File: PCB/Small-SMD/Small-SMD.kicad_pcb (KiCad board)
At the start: 2 copper layers, 65.1 x 96.9 mm, 28 parts, among them J1 Daisy port in, J3 UART, J4 Daisy port out, K1 HYC77-TF09-200, U1 PC817C-S, U2 SE5218, U21 TXB0104QPWRQ1

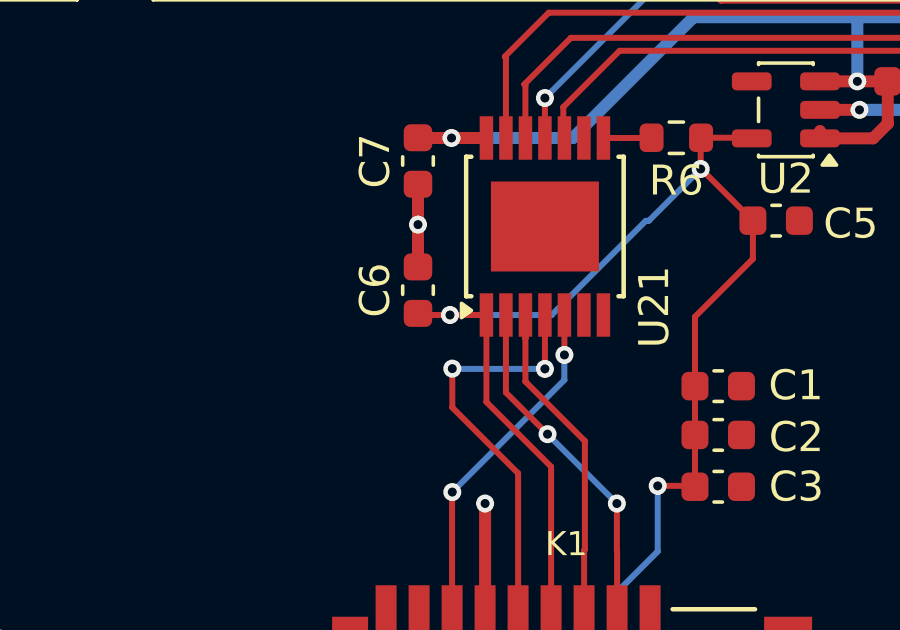
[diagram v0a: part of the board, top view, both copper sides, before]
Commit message: Switch to cheaper IDC box header
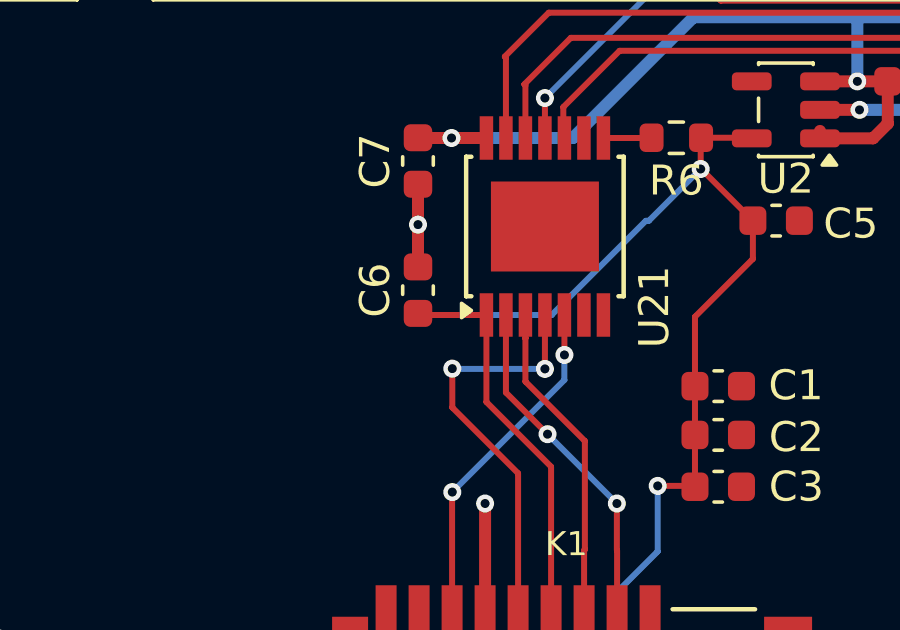
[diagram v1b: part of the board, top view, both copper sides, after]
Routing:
- net 3V3: vias 4 -> 3
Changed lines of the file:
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@@
-	)
-	(via
-		(at 115.5556 116.8078)
-		(size 0.6)
-		(drill 0.3)
-		(layers "F.Cu" "B.Cu")
-		(net 42)
 	)
 	(via

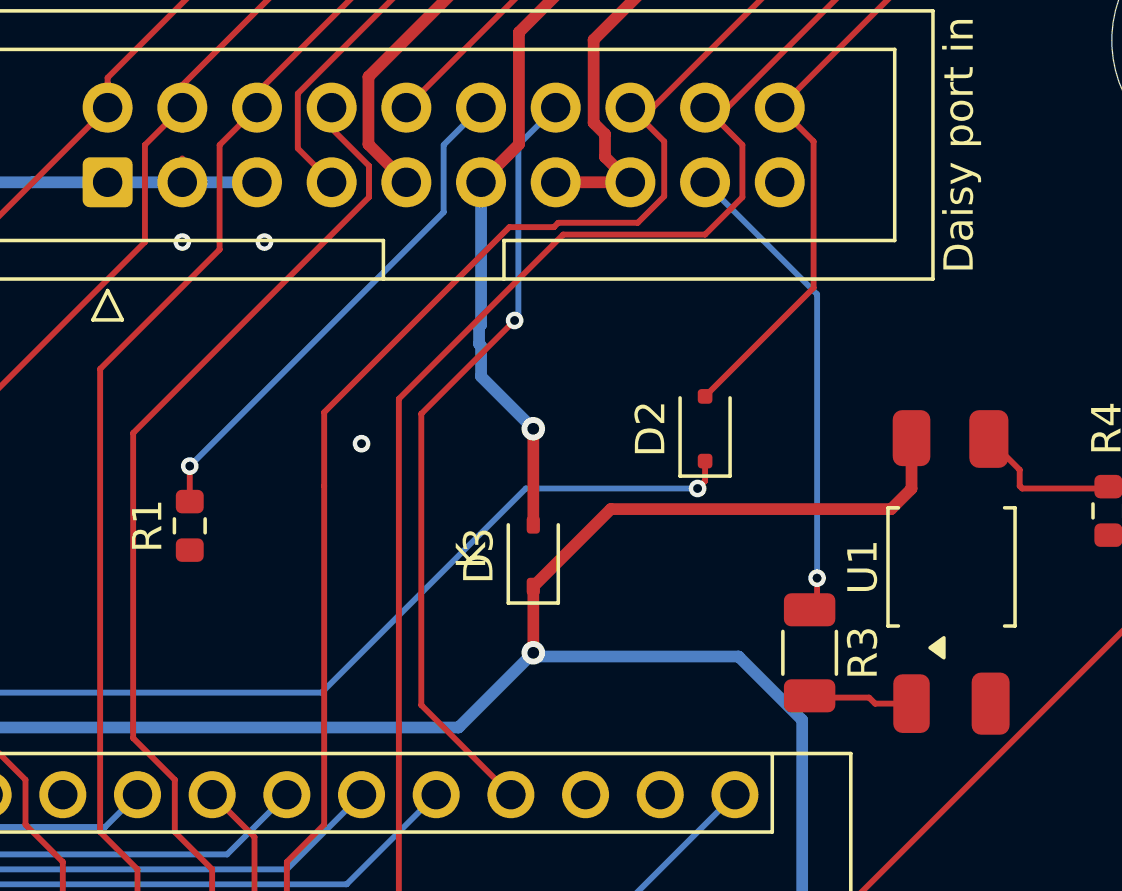
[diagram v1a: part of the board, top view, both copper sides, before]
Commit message: Fix U1 footprint
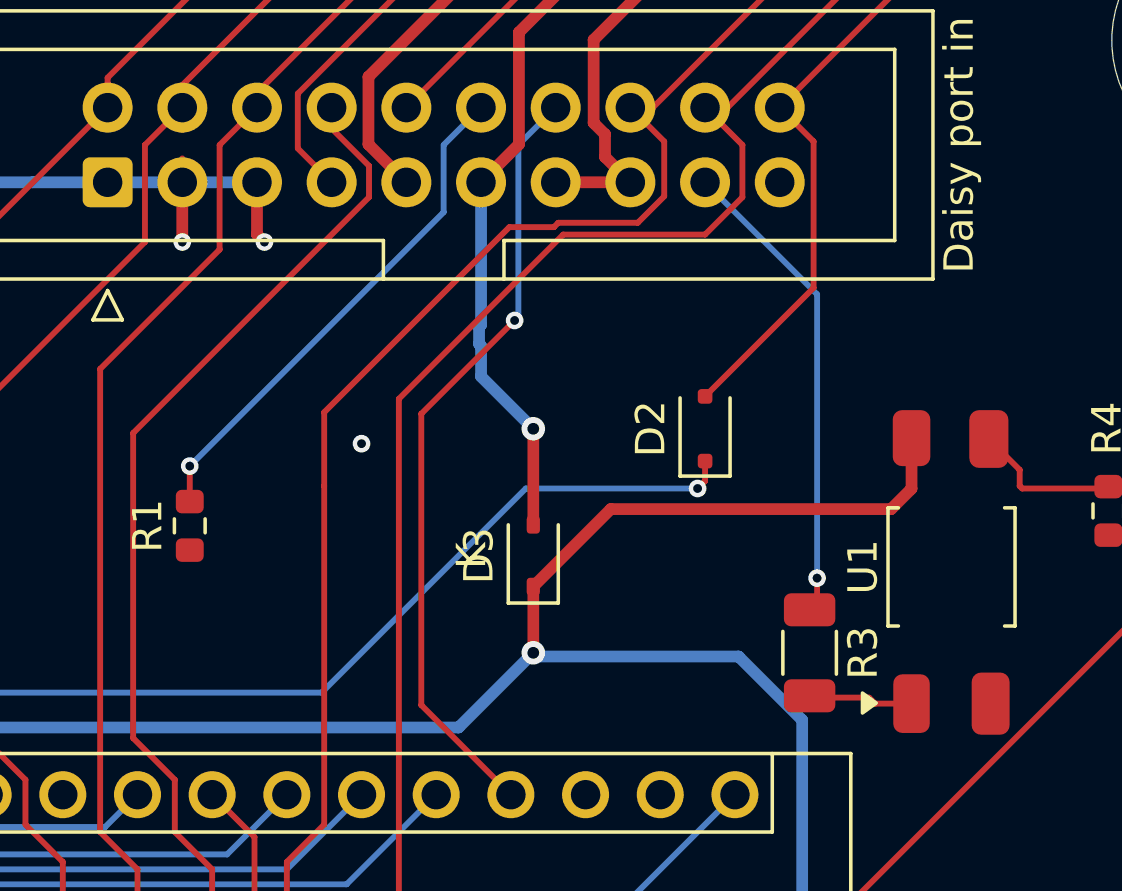
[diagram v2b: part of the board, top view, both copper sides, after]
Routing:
- net GND: track 47.9 -> 52.1 mm
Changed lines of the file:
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@@
 		(fp_poly
 			(pts
-				(xy -2.75 -0.73) (xy -2.41 -0.26) (xy -3.09 -0.26)
+				(xy -4.63 -2.56) (xy -4.97 -3.03) (xy -4.29 -3.03)
 			)
 			(stroke
@@
 			(layer "F.SilkS")
 		)
-		(fp_line
-			(start 5.5 -2.3)
-			(end 5.5 2.3)
-			(stroke
-				(width 0.05)
-				(type solid)
-			)
-			(layer "F.CrtYd")
-		)
-		(fp_line
-			(start 2.15 -2.3)
-			(end 5.5 -2.326172)
-			(stroke
-				(width 0.05)
-				(type solid)
-			)
-			(layer "F.CrtYd")
-		)
-		(fp_line
-			(start -2.15 -2.3)
-			(end 2.15 -2.3)
-			(stroke
-				(width 0.05)
-				(type solid)
-			)
-			(layer "F.CrtYd")
-		)
-		(fp_line
-			(start -5.719782 -2.3)
-			(end -2.15 -2.3)
-			(stroke
-				(width 0.05)
-				(type solid)
-			)
-			(layer "F.CrtYd")
-		)
-		(fp_line
-			(start 5.5 2.3)
-			(end 2.15 2.3)
-			(stroke
-				(width 0.05)
-				(type solid)
-			)
-			(layer "F.CrtYd")
-		)
-		(fp_line
-			(start 2.15 2.3)
-			(end -2.15 2.3)
-			(stroke
-				(width 0.05)
-				(type solid)
-			)
-			(layer "F.CrtYd")
-		)
-		(fp_line
-			(start -2.15 2.3)
-			(end -5.77 2.3)
+		(fp_rect
+			(start -5.78 -2.23)
+			(end 5.47 2.26)
 			(stroke
 				(width 0.05)
-				(type solid)
-			)
-			(layer "F.CrtYd")
-		)
-		(fp_line
-			(start -5.77 2.3)
-			(end -5.72 -2.28)
-			(stroke
-				(width 0.05)
-				(type solid)
+				(type default)
 			)
+			(fill no)
 			(layer "F.CrtYd")
 		)
@@
 	)
 	(segment
+		(start 123.952 70.866)
+		(end 123.698 70.612)
+		(width 0.4)
+		(layer "F.Cu")
+		(net 2)
+	)
+	(segment
+		(start 121.158 68.834)
+		(end 121.158 70.866)
+		(width 0.4)
+		(layer "F.Cu")
+		(net 2)
+	)
+	(segment
 		(start 131.6846 109.0328)
 		(end 131.6976 109.0198)
 		(width 0.4)
 		(layer "F.Cu")
+		(net 2)
+	)
+	(segment
+		(start 123.698 70.612)
+		(end 123.698 68.834)
+		(width 0.4)
+		(layer "F.Cu")

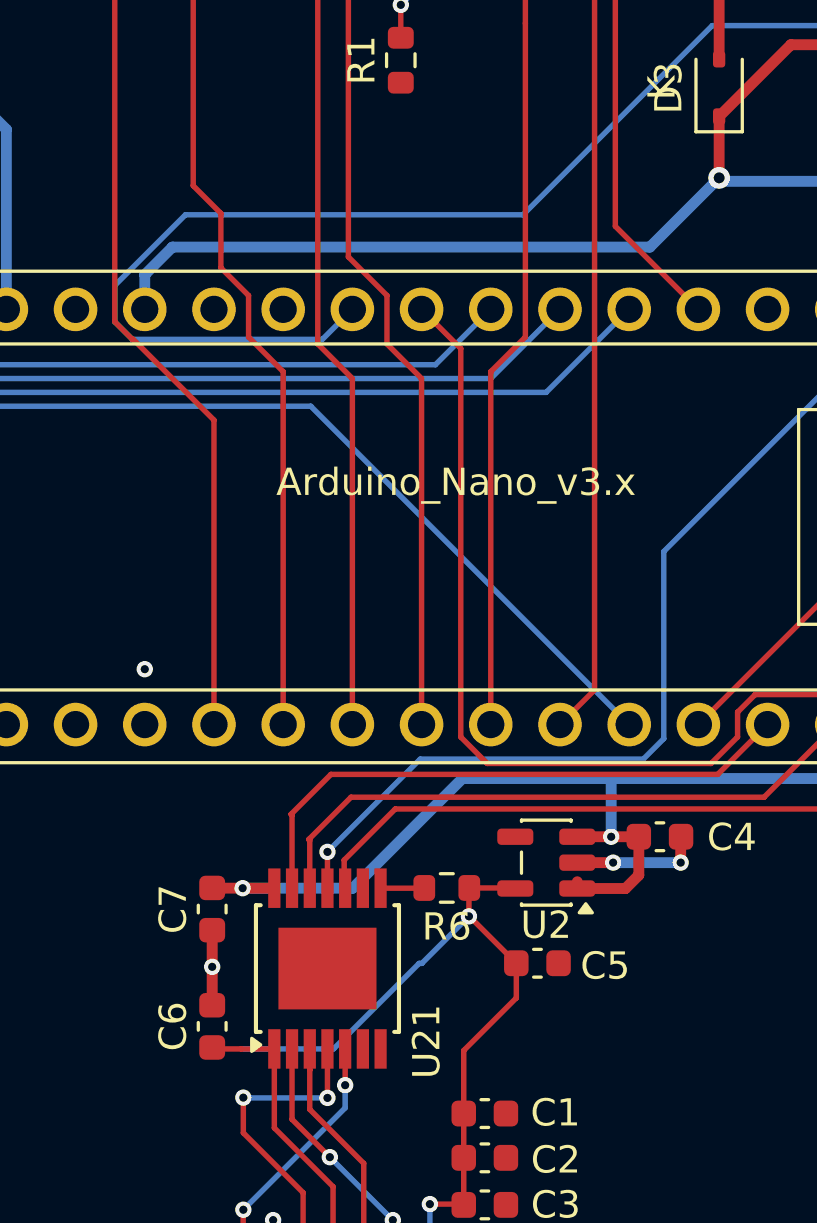
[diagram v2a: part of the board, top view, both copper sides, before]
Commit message: Add GND to level shifter :-/
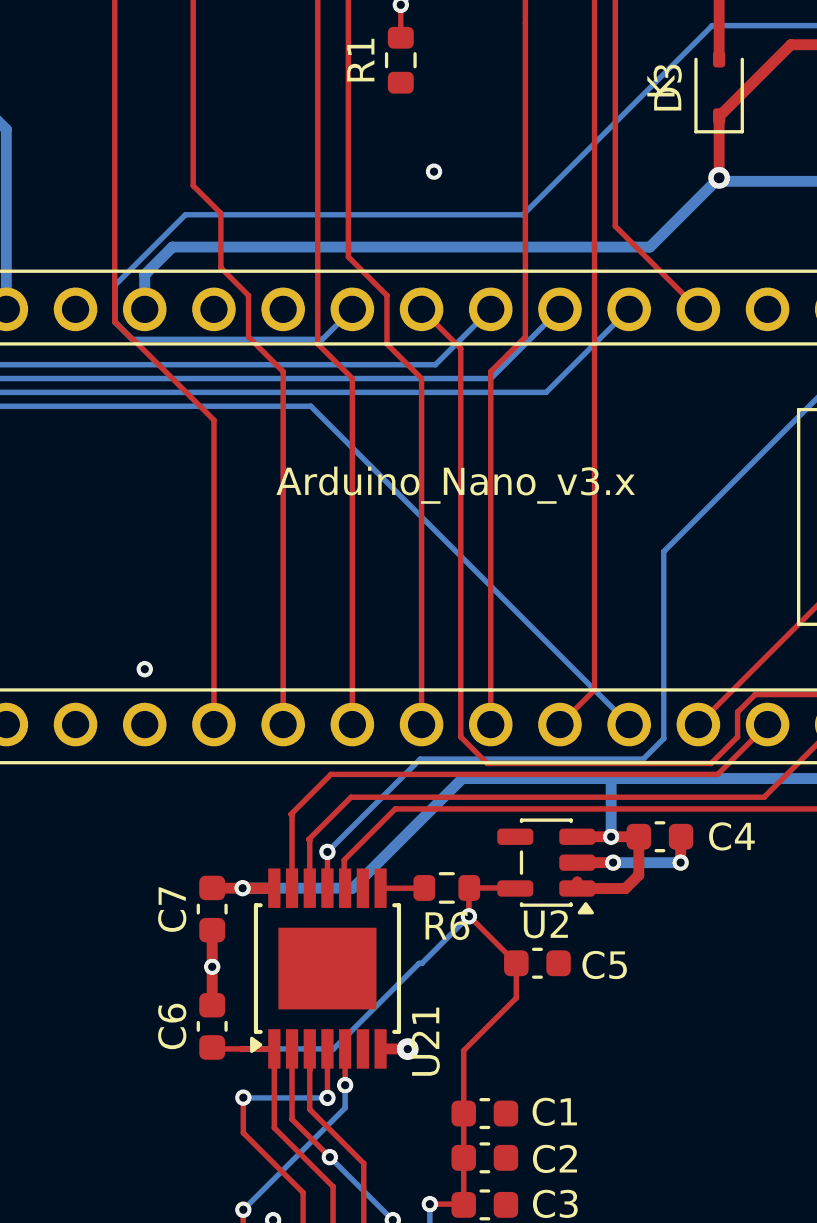
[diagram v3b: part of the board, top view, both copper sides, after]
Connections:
- U21 pad 7: unconnected-(U21-GND-Pad7) -> GND
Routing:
- net GND: track 52.1 -> 53.0 mm, vias 8 -> 10
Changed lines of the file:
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@@
 	(net 49 "OE")
 	(net 50 "unconnected-(U2-NC-Pad4)")
-	(net 51 "unconnected-(U21-GND-Pad7)")
-	(net 52 "unconnected-(U21-NC-Pad9)")
-	(net 53 "unconnected-(U21-NC-Pad6)")
+	(net 51 "unconnected-(U21-NC-Pad9)")
+	(net 52 "unconnected-(U21-NC-Pad6)")
 	(footprint "DSUB-19-angled:DSUB-19_Female_Horizontal_P2.77x2.84mm_EdgePinOffset4.94mm_Housed_MountingHolesOffset7.48mm"
 		(layer "F.Cu")
@@
 			(size 1.45 0.45)
 			(layers "F.Cu" "F.Mask" "F.Paste")
-			(net 53 "unconnected-(U21-NC-Pad6)")
+			(net 52 "unconnected-(U21-NC-Pad6)")
 			(pinfunction "NC")
 			(pintype "no_connect")
@@
 			(size 1.45 0.45)
 			(layers "F.Cu" "F.Mask" "F.Paste")
-			(net 51 "unconnected-(U21-GND-Pad7)")
+			(net 2 "GND")
 			(pinfunction "GND")
 			(pintype "passive")
@@
 			(size 1.45 0.45)
 			(layers "F.Cu" "F.Mask" "F.Paste")
-			(net 52 "unconnected-(U21-NC-Pad9)")
+			(net 51 "unconnected-(U21-NC-Pad9)")
 			(pinfunction "NC")
 			(pintype "no_connect")
@@
 			)
 		)
-		(property "LCSC" "C305958"
+		(property "LCSC" "C3405"
 			(at 167.386 -24.13 0)
 			(layer "F.Fab")
@@
 			)
 		)
-		(property "LCSC" "C258170"
+		(property "LCSC" "C167101"
 			(at 0 0 90)
 			(unlocked yes)
@@
 	)
 	(segment
+		(start 120.6696 116.8078)
+		(end 121.6592 116.8078)
+		(width 0.4)
+		(layer "F.Cu")
+		(net 2)
+	)
+	(segment
 		(start 131.6846 109.9698)
 		(end 131.6846 109.0328)
@@
 	)
 	(segment
+		(start 121.6592 116.8078)
+		(end 121.666 116.8146)
+		(width 0.4)
+		(layer "F.Cu")
+		(net 2)
+	)
+	(segment
 		(start 116.7252 126.616)
 		(end 116.7252 123.0914)
@@
 	)
 	(via
+		(at 121.666 116.8146)
+		(size 0.8)
+		(drill 0.3)
+		(layers "F.Cu" "B.Cu")
+		(net 2)
+	)
+	(via
 		(at 123.952 70.866)
 		(size 0.6)
@@
 		(net 2)
 	)
+	(via
+		(at 122.6312 84.6074)
+		(size 0.6)
+		(drill 0.3)
+		(layers "F.Cu" "B.Cu")
+		(free yes)
+		(net 2)
+	)

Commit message: WIP untested very small PCB
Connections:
- net Net-(A1-A4) renamed LED
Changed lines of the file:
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@@
 	(net 39 "HDSEL_in")
 	(net 40 "Net-(D4-A)")
-	(net 41 "Net-(A1-A4)")
+	(net 41 "LED")
 	(net 42 "3V3")
 	(net 43 "CS_L")
@@
 			(layers "*.Cu" "*.Mask")
 			(remove_unused_layers no)
-			(net 41 "Net-(A1-A4)")
+			(net 41 "LED")
 			(pinfunction "A4")
 			(pintype "bidirectional")
@@
 			(layers "F.Cu" "F.Mask" "F.Paste")
 			(roundrect_rratio 0.25)
-			(net 41 "Net-(A1-A4)")
+			(net 41 "LED")
 			(pintype "passive")
 		)
